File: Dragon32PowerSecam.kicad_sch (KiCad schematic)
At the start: 7 parts

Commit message: video tracing
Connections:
- net pl11_4: now reaches PL11.4
- net pl11_5: now reaches PL11.5
- net pl11_6: now reaches PL11.6
- net pl11_7: now reaches PL11.7
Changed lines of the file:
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@@
 	(generator_version "8.0")
 	(paper "A4")
+	(global_label "pl11_6"
+		(shape input)
+		(at 48.26 64.77 180)
+		(fields_autoplaced yes)
+		(effects
+			(font
+				(size 1.27 1.27)
+			)
+			(justify right)
+		)
+		(property "Intersheetrefs" "${INTERSHEET_REFS}"
+			(at 38.8645 64.77 0)
+			(effects
+				(font
+					(size 1.27 1.27)
+				)
+				(justify right)
+				(hide yes)
+			)
+		)
+	)
 	(global_label "phiA"
 		(shape input)
@@
 		)
 	)
+	(global_label "pl11_7"
+		(shape input)
+		(at 63.5 64.77 0)
+		(fields_autoplaced yes)
+		(effects
+			(font
+				(size 1.27 1.27)
+			)
+			(justify left)
+		)
+		(property "Intersheetrefs" "${INTERSHEET_REFS}"
+			(at 72.8955 64.77 0)
+			(effects
+				(font
+					(size 1.27 1.27)
+				)
+				(justify left)
+				(hide yes)
+			)
+		)
+	)
 	(global_label "LUMA"
 		(shape input)
@@
 		(property "Intersheetrefs" "${INTERSHEET_REFS}"
 			(at 144.5162 59.69 0)
+			(effects
+				(font
+					(size 1.27 1.27)
+				)
+				(justify right)
+				(hide yes)
+			)
+		)
+	)
+	(global_label "pl11_4"
+		(shape input)
+		(at 48.26 59.69 180)
+		(fields_autoplaced yes)
+		(effects
+			(font
+				(size 1.27 1.27)
+			)
+			(justify right)
+		)
+		(property "Intersheetrefs" "${INTERSHEET_REFS}"
+			(at 38.8645 59.69 0)
 			(effects
 				(font
@@
 				(hide yes)
 			)
+		)
+	)
+	(global_label "pl11_5"
+		(shape input)
+		(at 63.5 59.69 0)
+		(fields_autoplaced yes)
+		(effects
+			(font
+				(size 1.27 1.27)
+			)
+			(justify left)
+		)
+		(property "Intersheetrefs" "${INTERSHEET_REFS}"
+			(at 72.8955 59.69 0)
+			(effects
+				(font
+					(size 1.27 1.27)
+				)
+				(justify left)
+				(hide yes)
+			)

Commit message: more video tracing
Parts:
- removed PL9: DE9_Plug_MountingHoles, Connector_Dsub:DSUB-9_Male_Horizontal_P2.77x2.84mm_EdgePinOffset9.90mm_Housed_MountingHolesOffset11.32mm, symbol Connector:DE9_Plug_MountingHoles
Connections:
- net pl11_1: now reaches PL11.1
- net pl11_2: now reaches PL11.2
- net pl11_3: now reaches PL11.3
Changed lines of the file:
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@@
 	(generator_version "8.0")
 	(paper "A4")
+	(global_label "pl11_3"
+		(shape input)
+		(at 63.5 62.23 0)
+		(fields_autoplaced yes)
+		(effects
+			(font
+				(size 1.27 1.27)
+			)
+			(justify left)
+		)
+		(property "Intersheetrefs" "${INTERSHEET_REFS}"
+			(at 72.8955 62.23 0)
+			(effects
+				(font
+					(size 1.27 1.27)
+				)
+				(justify left)
+				(hide yes)
+			)
+		)
+	)
 	(global_label "pl11_6"
 		(shape input)
@@
 		(property "Intersheetrefs" "${INTERSHEET_REFS}"
 			(at 72.8955 59.69 0)
+			(effects
+				(font
+					(size 1.27 1.27)
+				)
+				(justify left)
+				(hide yes)
+			)
+		)
+	)
+	(global_label "pl11_1"
+		(shape input)
+		(at 48.26 62.23 180)
+		(fields_autoplaced yes)
+		(effects
+			(font
+				(size 1.27 1.27)
+			)
+			(justify right)
+		)
+		(property "Intersheetrefs" "${INTERSHEET_REFS}"
+			(at 38.8645 62.23 0)
+			(effects
+				(font
+					(size 1.27 1.27)
+				)
+				(justify right)
+				(hide yes)
+			)
+		)
+	)
+	(global_label "pl11_2"
+		(shape input)
+		(at 55.88 54.61 90)
+		(fields_autoplaced yes)
+		(effects
+			(font
+				(size 1.27 1.27)
+			)
+			(justify left)
+		)
+		(property "Intersheetrefs" "${INTERSHEET_REFS}"
+			(at 55.88 45.2145 90)
 			(effects
 				(font
@@
 					(unit 1)
 				)
-			)
-		)
-	)
-	(symbol
-		(lib_id "Connector:DE9_Plug_MountingHoles")
-		(at 218.44 35.56 0)
-		(unit 1)
-		(exclude_from_sim no)
-		(in_bom yes)
-		(on_board yes)
-		(dnp no)
-		(fields_autoplaced yes)
-		(property "Reference" "PL9"
-			(at 223.52 34.2899 0)
-			(effects
-				(font
-					(size 1.27 1.27)
-				)
-				(justify left)
-			)
-		)
-		(property "Value" "DE9_Plug_MountingHoles"
-			(at 223.52 36.8299 0)
-			(effects
-				(font
-					(size 1.27 1.27)
-				)
-				(justify left)
-			)
-		)
-		(property "Footprint" "Connector_Dsub:DSUB-9_Male_Horizontal_P2.77x2.84mm_EdgePinOffset9.90mm_Housed_MountingHolesOffset11.32mm"
-			(at 218.44 35.56 0)
-			(effects
-				(font
-					(size 1.27 1.27)
-				)
-				(hide yes)
-			)
-		)
-		(property "Datasheet" "~"
-			(at 218.44 35.56 0)
-			(effects
-				(font
-					(size 1.27 1.27)
-				)
-				(hide yes)
-			)
-		)
-		(property "Description" "9-pin male plug pin D-SUB connector, Mounting Hole"
-			(at 218.44 35.56 0)
-			(effects
-				(font
-					(size 1.27 1.27)
-				)
-				(hide yes)
-			)
-		)
-		(pin "1"
-		)
-		(pin "4"
-		)
-		(pin "9"
-		)
-		(pin "2"
-		)
-		(pin "7"
-		)
-		(pin "0"
-		)
-		(pin "3"
-		)
-		(pin "5"
-		)
-		(pin "6"
-		)
-		(pin "8"
-		)
-		(instances
-			(project ""
-				(path "/ace185c2-9b54-41ba-956b-7e7c726e18a3"
-					(reference "PL9")
-					(unit 1)
-				)

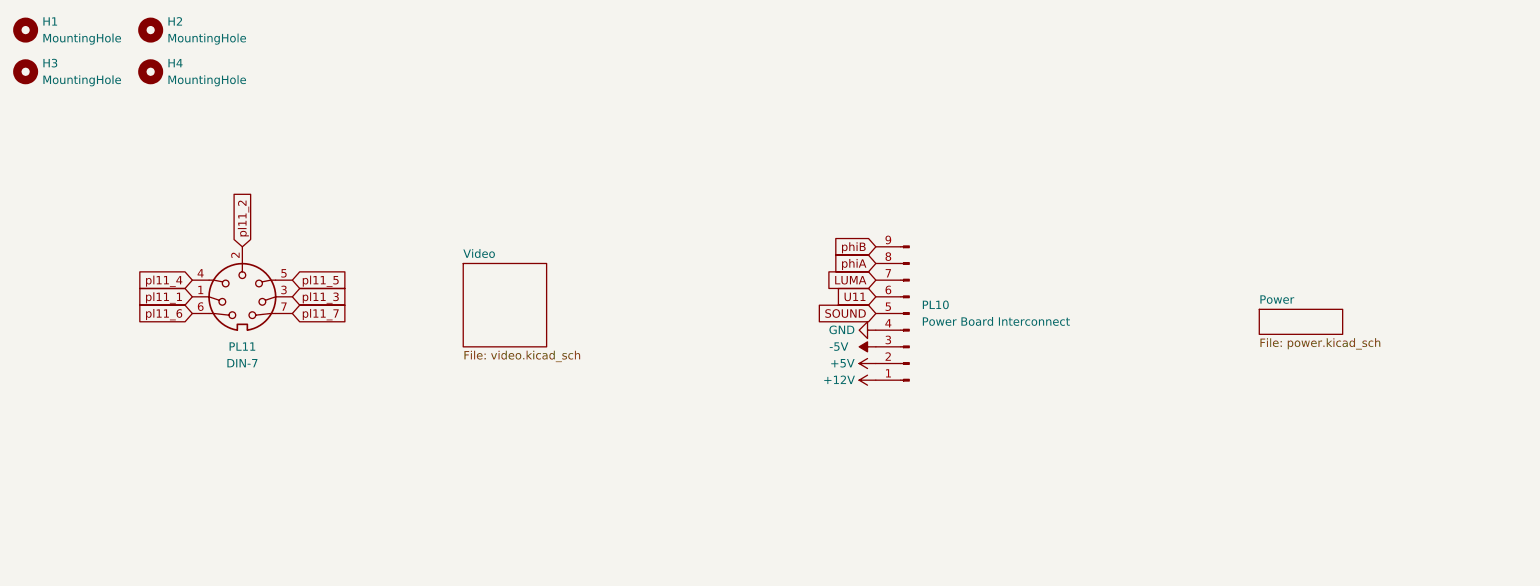
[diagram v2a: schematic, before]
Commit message: rationalise rgb circuit
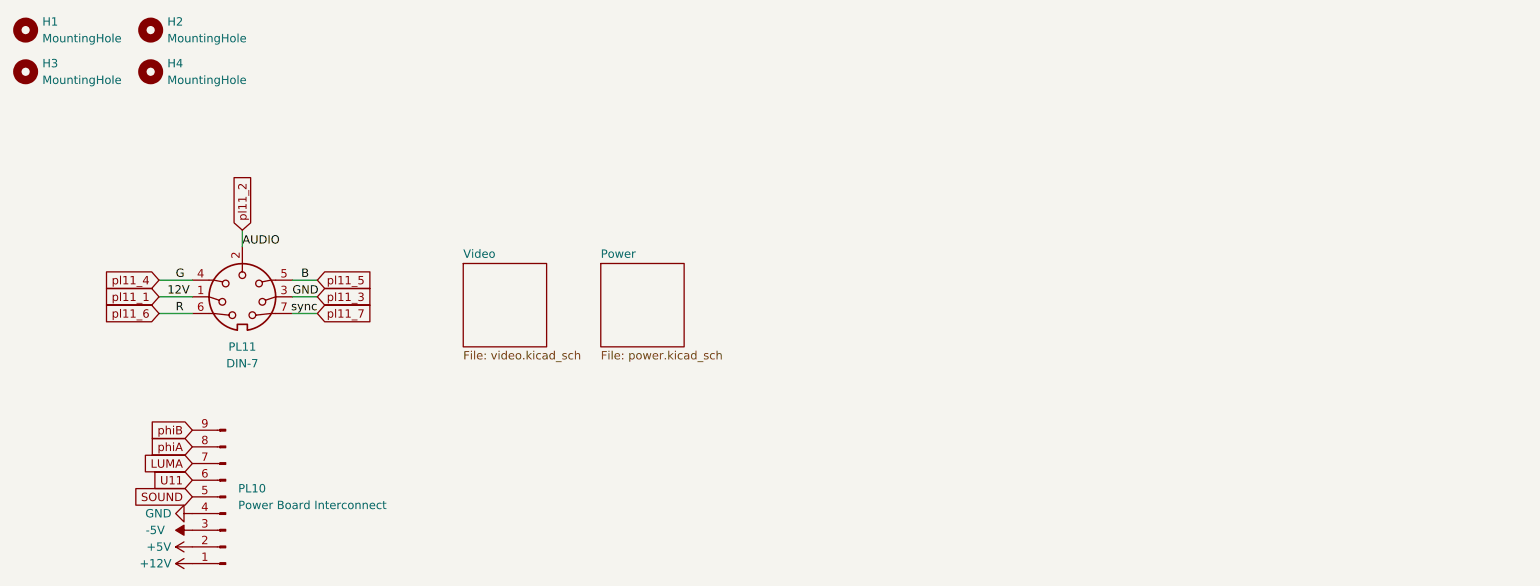
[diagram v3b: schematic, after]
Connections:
- net pl11_3 is gone; now on net GND: PL11.3
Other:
- moved on the sheet: PL10

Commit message: update labelling
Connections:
- net U11 renamed SECAM_COMP
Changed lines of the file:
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@@
 		)
 	)
-	(label "AUDIO"
+	(label "5V"
 		(at 55.88 54.61 0)
 		(effects
@@
 		)
 	)
-	(global_label "U11"
+	(global_label "SECAM_COMP"
 		(shape input)
 		(at 48.26 90.17 180)
@@
 		)
 		(property "Intersheetrefs" "${INTERSHEET_REFS}"
-			(at 41.5253 90.17 0)
-			(effects
-				(font
+			(at 32.8168 90.17 0)
+			(effects
+				(font
